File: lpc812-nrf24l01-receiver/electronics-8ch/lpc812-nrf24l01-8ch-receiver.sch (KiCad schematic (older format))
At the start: 23 parts, among them J1 CH1, J2 CH2, J3 CH3/Rx, J4 CH4/Tx, J5 CH5, J6 CH6, J7 CH7, J8 CH8, SW1 BIND/ISP, U1 MCP1703A-3302_SOT23, U2 LPC812M101JDH20, U3 NRF24L01_E01_ML01, Y1 12 MHz

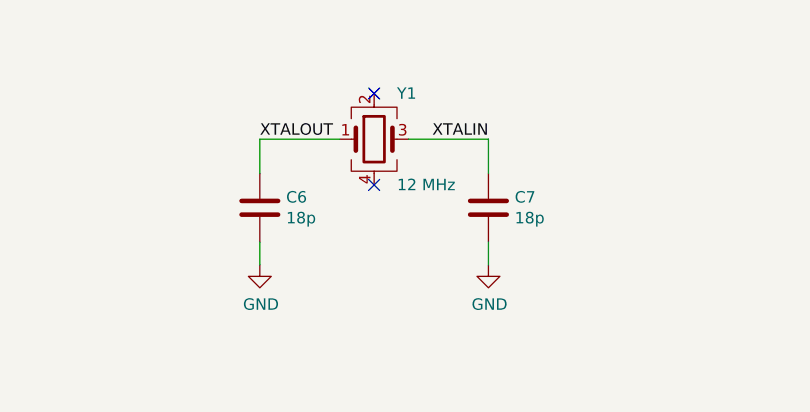
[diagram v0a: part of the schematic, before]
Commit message: Change crystal of 8ch version to 16 MHz
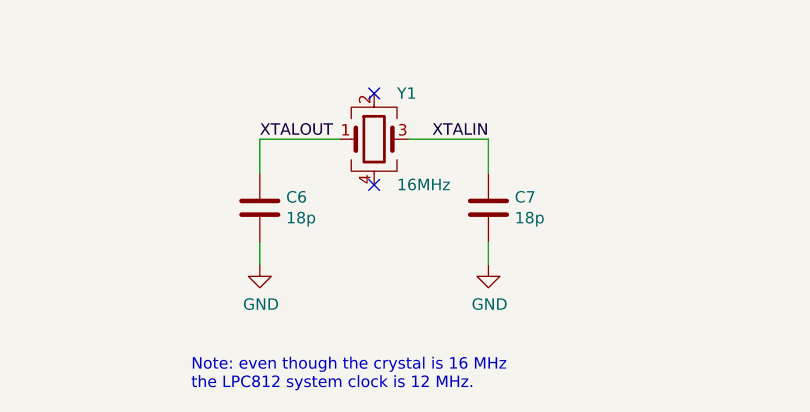
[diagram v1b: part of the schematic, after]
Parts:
- Y1: value 12 MHz -> 16MHz
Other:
- note added: "Note: even though the crystal is 16 MHz\nthe LPC812 system clock is 12 MHz."
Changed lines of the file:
@@
 P 5600 6250
 F 0 "Y1" H 5700 6450 50  0000 L CNN
-F 1 "12 MHz" H 5700 6050 50  0000 L CNN
+F 1 "16MHz" H 5700 6050 50  0000 L CNN
 F 2 "Crystal:Crystal_SMD_2520-4Pin_2.5x2.0mm" H 5600 6250 50  0001 C CNN
 F 3 "~" H 5600 6250 50  0001 C CNN
@@
 NoConn ~ 5600 6450
 NoConn ~ 5600 6050
+Text Notes 4800 7350 0    50   ~ 0
+Note: even though the crystal is 16 MHz\nthe LPC812 system clock is 12 MHz.
 $EndSCHEMATC

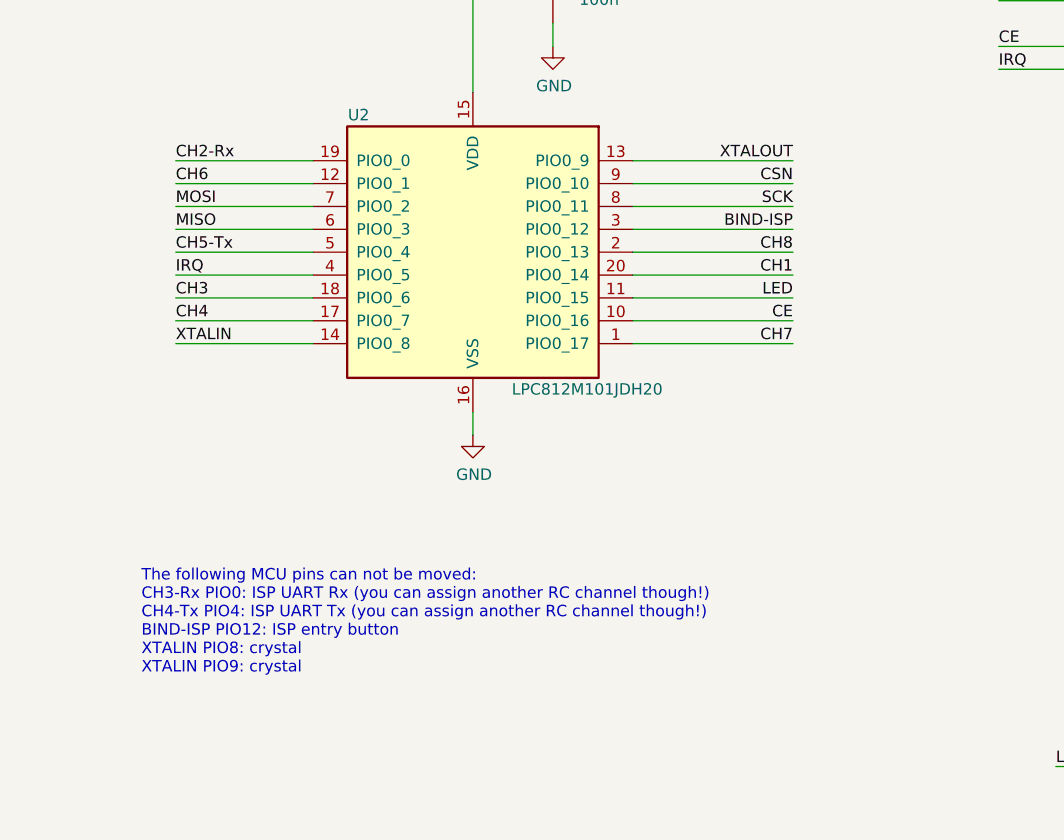
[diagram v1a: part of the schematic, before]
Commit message: Make PIO10 and PIO11 use as input pins as they are open drain
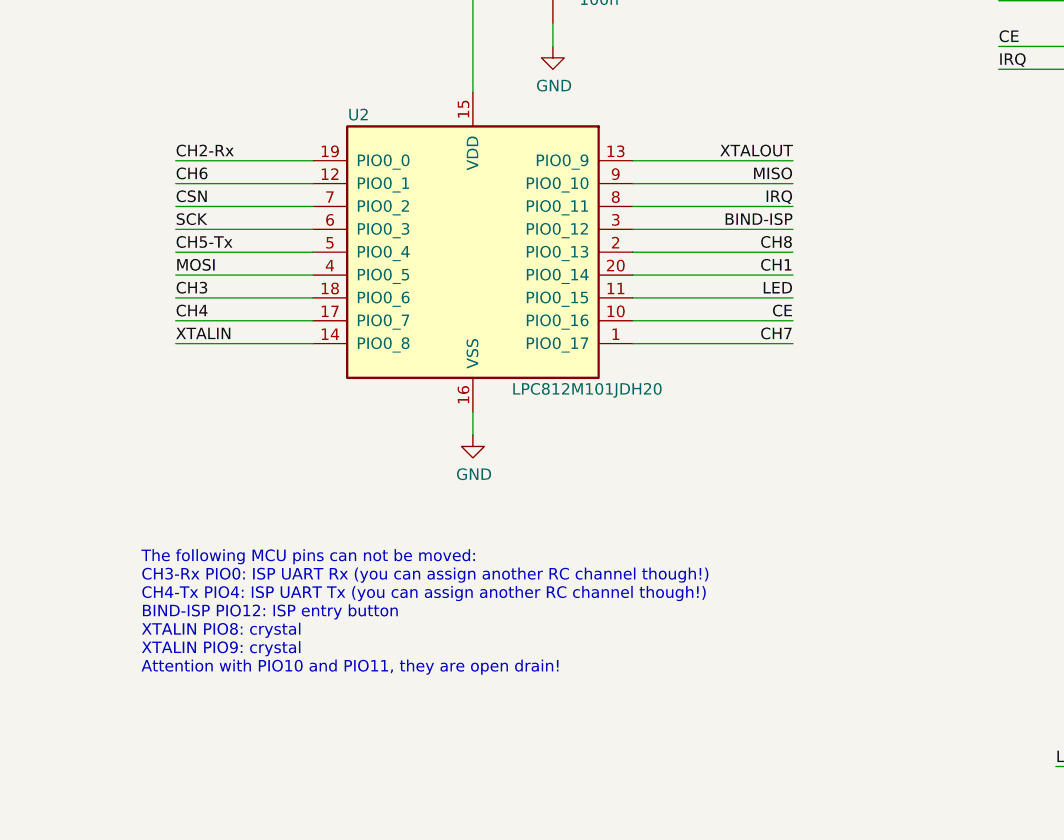
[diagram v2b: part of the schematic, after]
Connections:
- net CSN: now also U2.7 (PIO0_2); no longer U2.9 (PIO0_10)
- net IRQ: now also U2.8 (PIO0_11); no longer U2.4 (PIO0_5)
- net MISO: now also U2.9 (PIO0_10); no longer U2.6 (PIO0_3)
- net MOSI: now also U2.4 (PIO0_5); no longer U2.7 (PIO0_2)
- net SCK: now also U2.6 (PIO0_3); no longer U2.8 (PIO0_11)
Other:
- note added: "The following MCU pins can not be moved:\nCH3-Rx PIO0: ISP UART Rx (you can assign another RC channel though!)\nCH4-Tx PIO4: ISP UART Tx (you can assign another RC channel though!)\nBIND-ISP PIO12: ISP entry button\nXTALIN PIO8: crystal\nXTALIN PIO9: crystal\nAttention with PIO10 and PIO11, they are open drain!"
- note removed: "The following MCU pins can not be moved:\nCH3-Rx PIO0: ISP UART Rx (you can assign another RC channel though!)\nCH4-Tx PIO4: ISP UART Tx (you can assign another RC channel though!)\nBIND-ISP PIO12: ISP entry button\nXTALIN PIO8: crystal\nXTALIN PIO9: crystal"
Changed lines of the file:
@@
 CH6
 Text Label 1900 2900 0    50   ~ 0
-MOSI
+CSN
 Text Label 1900 3000 0    50   ~ 0
-MISO
+SCK
 Text Label 1900 3100 0    50   ~ 0
 CH5-Tx
 Text Label 1900 3200 0    50   ~ 0
-IRQ
+MOSI
 Text Label 1900 3300 0    50   ~ 0
 CH3
@@
 	3900 2800 4600 2800
 Text Label 4600 2800 2    50   ~ 0
-CSN
+MISO
 Wire Wire Line
 	3900 2900 4600 2900
@@
 	3900 3000 4600 3000
 Text Label 4600 2900 2    50   ~ 0
-SCK
+IRQ
 Text Label 4600 3000 2    50   ~ 0
 BIND-ISP
@@
 	10000 6100 10000 6200
 Text Notes 1750 4950 0    50   ~ 0
-The following MCU pins can not be moved:\nCH3-Rx PIO0: ISP UART Rx (you can assign another RC channel though!)\nCH4-Tx PIO4: ISP UART Tx (you can assign another RC channel though!)\nBIND-ISP PIO12: ISP entry button\nXTALIN PIO8: crystal\nXTALIN PIO9: crystal
+The following MCU pins can not be moved:\nCH3-Rx PIO0: ISP UART Rx (you can assign another RC channel though!)\nCH4-Tx PIO4: ISP UART Tx (you can assign another RC channel though!)\nBIND-ISP PIO12: ISP entry button\nXTALIN PIO8: crystal\nXTALIN PIO9: crystal\nAttention with PIO10 and PIO11, they are open drain!
 $Comp
 L nrf24l01_E01-ML01:NRF24L01_E01_ML01 U3

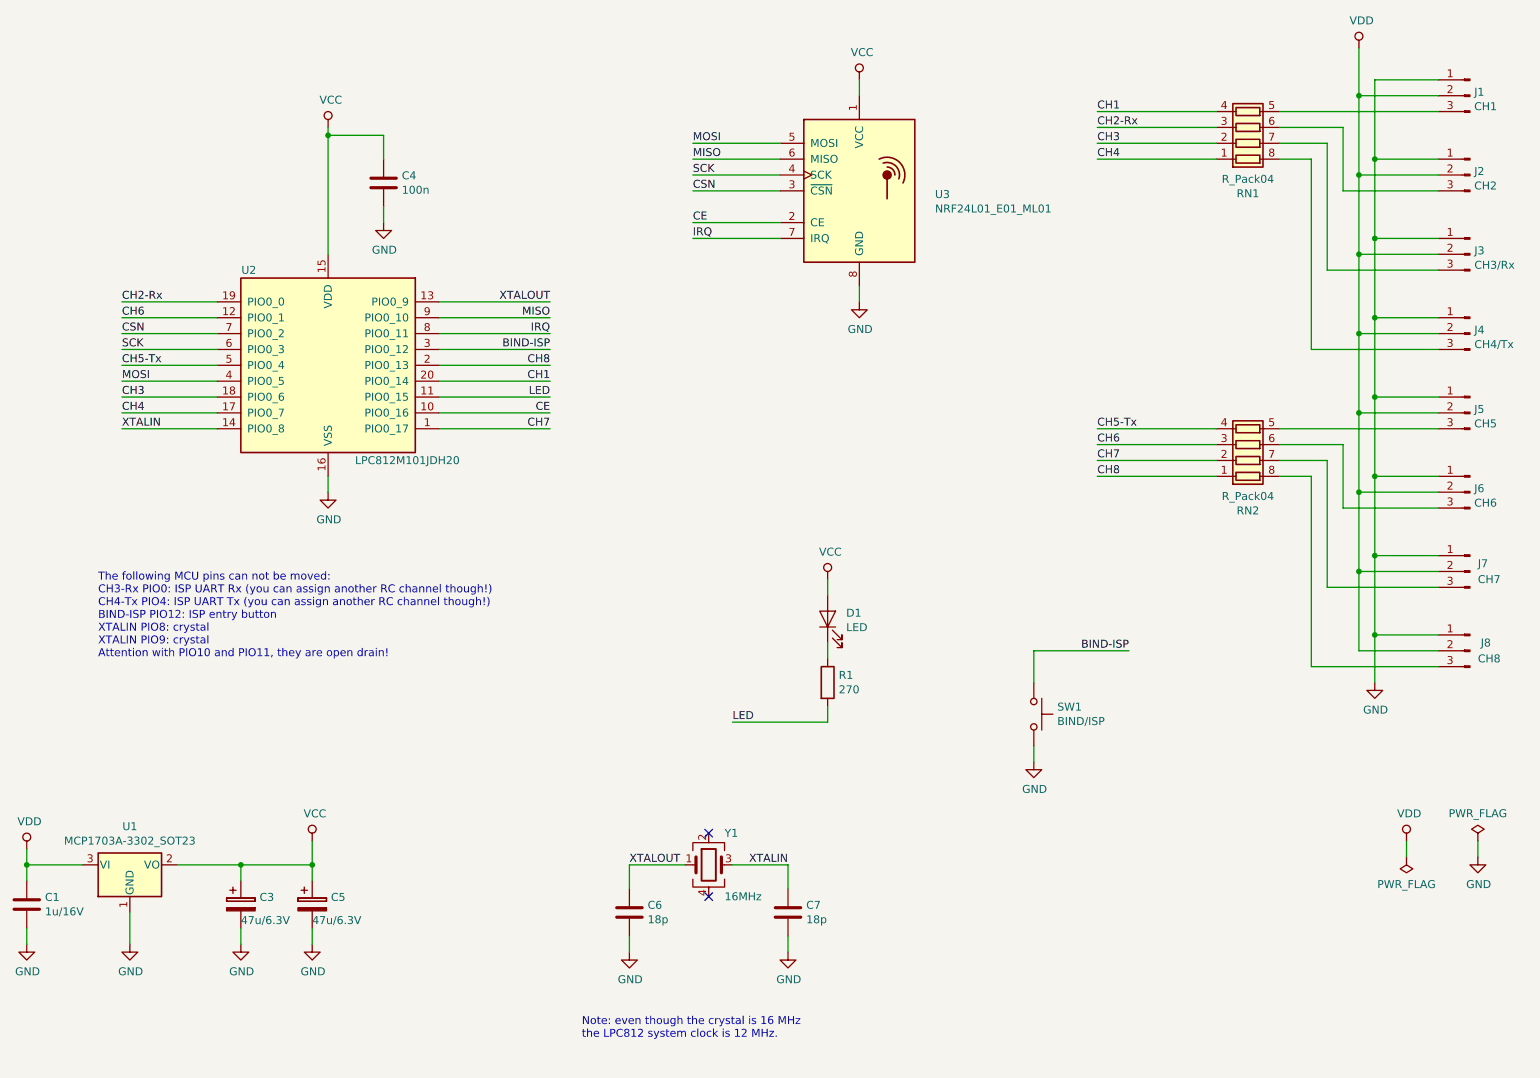
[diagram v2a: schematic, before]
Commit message: Change crystal to 12 MHz and add schematics annotations
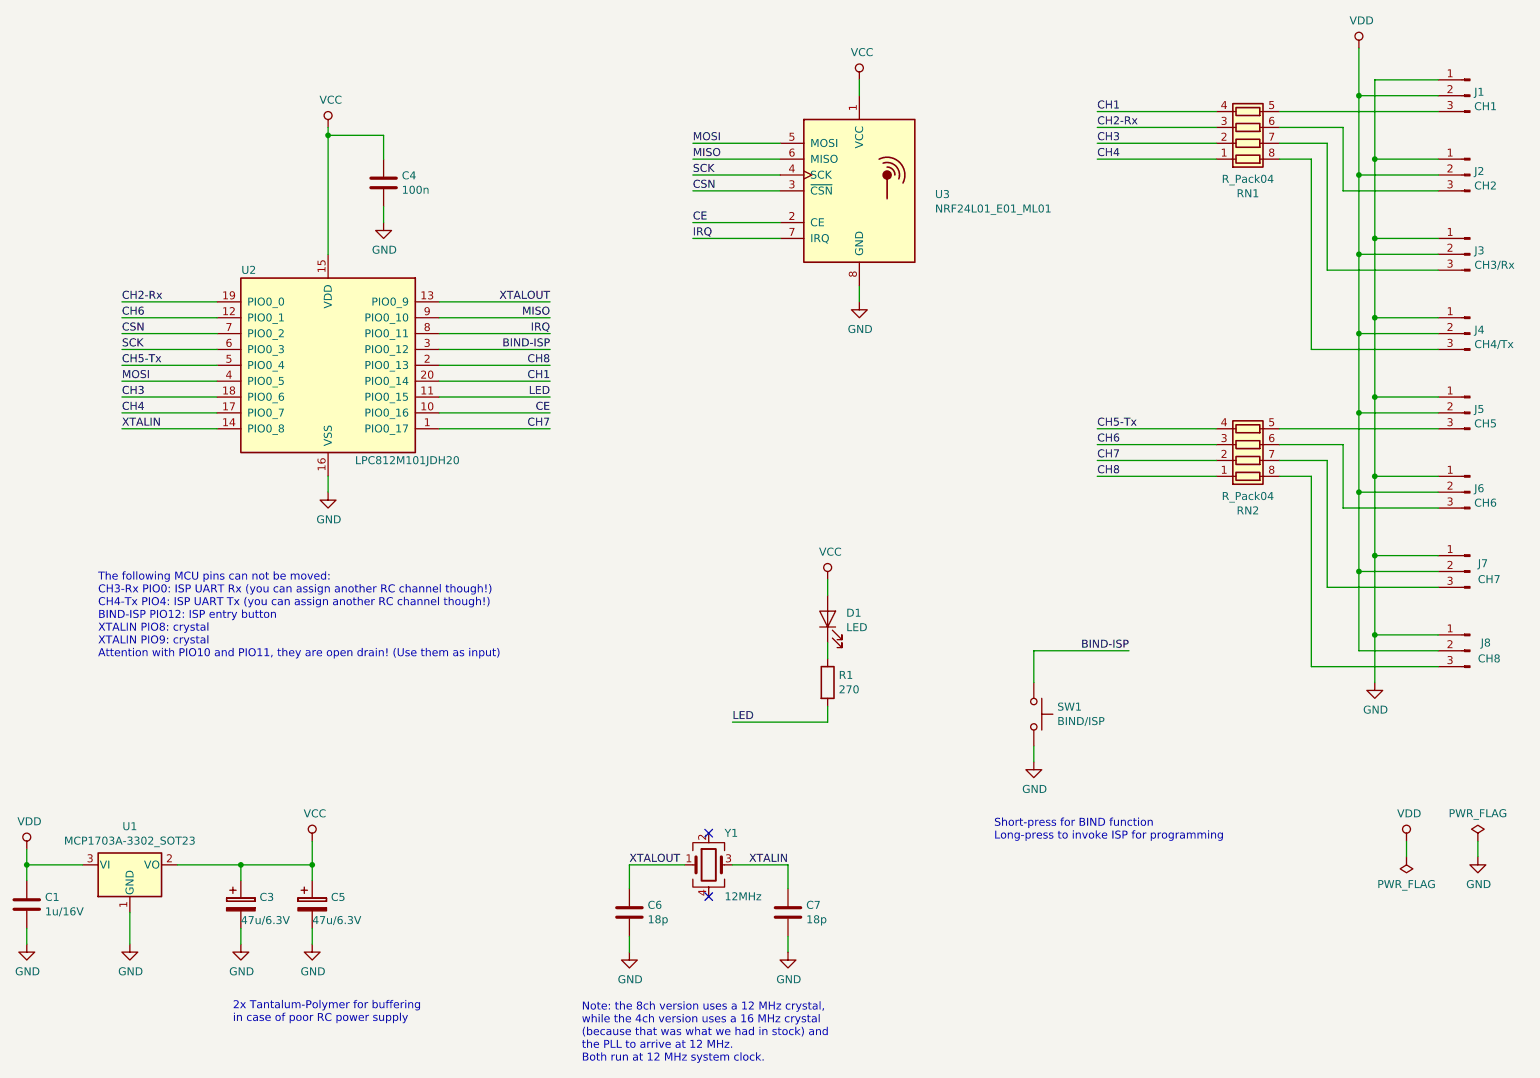
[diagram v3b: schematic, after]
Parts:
- Y1: value 16MHz -> 12MHz
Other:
- note added: "2x Tantalum-Polymer for buffering \nin case of poor RC power supply"
- note added: "Note: the 8ch version uses a 12 MHz crystal,\nwhile the 4ch version uses a 16 MHz crystal \n(because that was what we had in stock) and \nthe PLL to arrive at 12 MHz.\nBoth run at 12 MHz system clock."
- note added: "Short-press for BIND function\nLong-press to invoke ISP for programming"
- note added: "The following MCU pins can not be moved:\nCH3-Rx PIO0: ISP UART Rx (you can assign another RC channel though!)\nCH4-Tx PIO4: ISP UART Tx (you can assign another RC channel though!)\nBIND-ISP PIO12: ISP entry button\nXTALIN PIO8: crystal\nXTALIN PIO9: crystal\nAttention with PIO10 and PIO11, they are open drain! (Use them as input)"
- note removed: "Note: even though the crystal is 16 MHz\nthe LPC812 system clock is 12 MHz."
- note removed: "The following MCU pins can not be moved:\nCH3-Rx PIO0: ISP UART Rx (you can assign another RC channel though!)\nCH4-Tx PIO4: ISP UART Tx (you can assign another RC channel though!)\nBIND-ISP PIO12: ISP entry button\nXTALIN PIO8: crystal\nXTALIN PIO9: crystal\nAttention with PIO10 and PIO11, they are open drain!"
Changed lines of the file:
@@
 encoding utf-8
 Sheet 1 1
-Title ""
-Date ""
-Rev ""
-Comp ""
+Title "LPC812 / nRF24L01P based 8-channel receiver"
+Date "2018-09-29"
+Rev "1"
+Comp "LANE Boys RC"
 Comment1 ""
 Comment2 ""
@@
 	10000 6100 10000 6200
 Text Notes 1750 4950 0    50   ~ 0
-The following MCU pins can not be moved:\nCH3-Rx PIO0: ISP UART Rx (you can assign another RC channel though!)\nCH4-Tx PIO4: ISP UART Tx (you can assign another RC channel though!)\nBIND-ISP PIO12: ISP entry button\nXTALIN PIO8: crystal\nXTALIN PIO9: crystal\nAttention with PIO10 and PIO11, they are open drain!
+The following MCU pins can not be moved:\nCH3-Rx PIO0: ISP UART Rx (you can assign another RC channel though!)\nCH4-Tx PIO4: ISP UART Tx (you can assign another RC channel though!)\nBIND-ISP PIO12: ISP entry button\nXTALIN PIO8: crystal\nXTALIN PIO9: crystal\nAttention with PIO10 and PIO11, they are open drain! (Use them as input)
 $Comp
 L nrf24l01_E01-ML01:NRF24L01_E01_ML01 U3
@@
 P 5600 6250
 F 0 "Y1" H 5700 6450 50  0000 L CNN
-F 1 "16MHz" H 5700 6050 50  0000 L CNN
+F 1 "12MHz" H 5700 6050 50  0000 L CNN
 F 2 "Crystal:Crystal_SMD_2520-4Pin_2.5x2.0mm" H 5600 6250 50  0001 C CNN
 F 3 "~" H 5600 6250 50  0001 C CNN
@@
 NoConn ~ 5600 6450
 NoConn ~ 5600 6050
-Text Notes 4800 7350 0    50   ~ 0
-Note: even though the crystal is 16 MHz\nthe LPC812 system clock is 12 MHz.
+Text Notes 4800 7500 0    50   ~ 0
+Note: the 8ch version uses a 12 MHz crystal,\nwhile the 4ch version uses a 16 MHz crystal \n(because that was what we had in stock) and \nthe PLL to arrive at 12 MHz.\nBoth run at 12 MHz system clock.
+Text Notes 2600 7250 0    50   ~ 0
+2x Tantalum-Polymer for buffering \nin case of poor RC power supply
+Text Notes 7400 6100 0    50   ~ 0
+Short-press for BIND function\nLong-press to invoke ISP for programming
 $EndSCHEMATC

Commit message: Tidy up Fab layer
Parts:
- RN1, RN2: value R_Pack04 -> 1k x 4
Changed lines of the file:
@@
 P 9000 1600
 F 0 "RN1" V 8583 1600 50  0000 C CNN
-F 1 "R_Pack04" V 8674 1600 50  0000 C CNN
+F 1 "1k x 4" V 8674 1600 50  0000 C CNN
 F 2 "Resistor_SMD:R_Array_Concave_4x0603" V 9275 1600 50  0001 C CNN
 F 3 "~" H 9000 1600 50  0001 C CNN
@@
 P 9000 3600
 F 0 "RN2" V 8583 3600 50  0000 C CNN
-F 1 "R_Pack04" V 8674 3600 50  0000 C CNN
+F 1 "1k x 4" V 8674 3600 50  0000 C CNN
 F 2 "Resistor_SMD:R_Array_Concave_4x0603" V 9275 3600 50  0001 C CNN
 F 3 "~" H 9000 3600 50  0001 C CNN

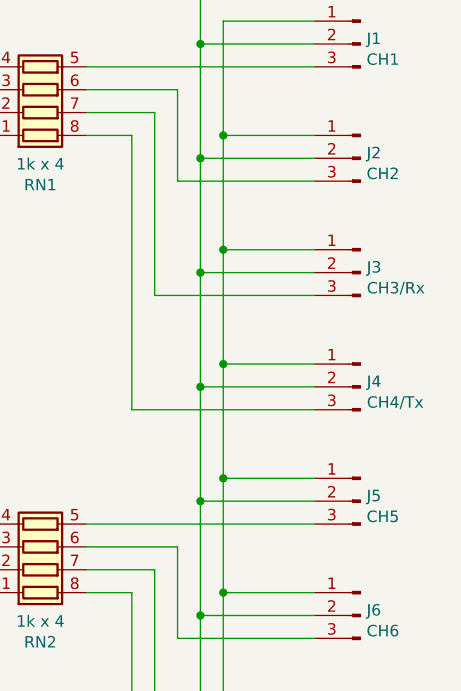
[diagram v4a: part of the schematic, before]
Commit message: Fix connector label
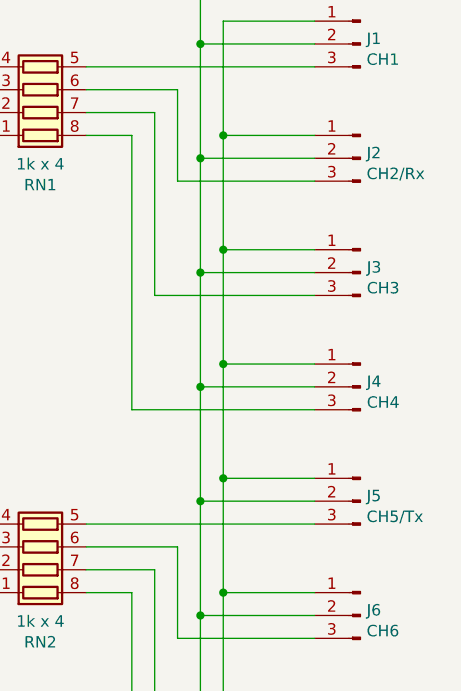
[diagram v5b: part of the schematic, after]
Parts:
- J2: value CH2 -> CH2/Rx
- J3: value CH3/Rx -> CH3
- J4: value CH4/Tx -> CH4
- J5: value CH5 -> CH5/Tx
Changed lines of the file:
@@
 P 10400 3400
 F 0 "J5" H 10373 3423 50  0000 R CNN
-F 1 "CH5" H 10373 3332 50  0000 R CNN
+F 1 "CH5/Tx" H 10373 3332 50  0000 R CNN
 F 2 "Connector_PinHeader_2.54mm:PinHeader_1x03_P2.54mm_Vertical" H 10400 3400 50  0001 C CNN
 F 3 "~" H 10400 3400 50  0001 C CNN
@@
 P 10400 1900
 F 0 "J2" H 10373 1923 50  0000 R CNN
-F 1 "CH2" H 10373 1832 50  0000 R CNN
+F 1 "CH2/Rx" H 10373 1832 50  0000 R CNN
 F 2 "Connector_PinHeader_2.54mm:PinHeader_1x03_P2.54mm_Vertical" H 10400 1900 50  0001 C CNN
 F 3 "~" H 10400 1900 50  0001 C CNN
@@
 P 10400 2400
 F 0 "J3" H 10372 2423 50  0000 R CNN
-F 1 "CH3/Rx" H 10372 2332 50  0000 R CNN
+F 1 "CH3" H 10372 2332 50  0000 R CNN
 F 2 "Connector_PinHeader_2.54mm:PinHeader_1x03_P2.54mm_Vertical" H 10400 2400 50  0001 C CNN
 F 3 "~" H 10400 2400 50  0001 C CNN
@@
 P 10400 2900
 F 0 "J4" H 10372 2923 50  0000 R CNN
-F 1 "CH4/Tx" H 10372 2832 50  0000 R CNN
+F 1 "CH4" H 10372 2832 50  0000 R CNN
 F 2 "Connector_PinHeader_2.54mm:PinHeader_1x03_P2.54mm_Vertical" H 10400 2900 50  0001 C CNN
 F 3 "~" H 10400 2900 50  0001 C CNN
